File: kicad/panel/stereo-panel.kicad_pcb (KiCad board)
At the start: 2 copper layers, 134.1 x 137.1 mm, 235 parts, among them J1 AC IN 12-15V, J1 DC 12V IN, J1 IN L-G-R, J2 DC IN 12V, J2 IN L-G-R, J2 OUT L-G-R, J3 DC OUT 1, J3 LED IN, J3 SPK L, J4 DC OUT 2, J4 SPK R, J5 LED REMOTE, Q1 BC547, Q1001 BC547, Q1002 BC547, Q1003 BC557, Q1004 BD139, Q1005 BD140, Q1006 BC547, Q2 TIP41C, Q2001 BC547, Q2002 BC547, Q2003 BC557, Q2004 BD139, Q2005 BD140, Q2006 BC547, Q3 BC547

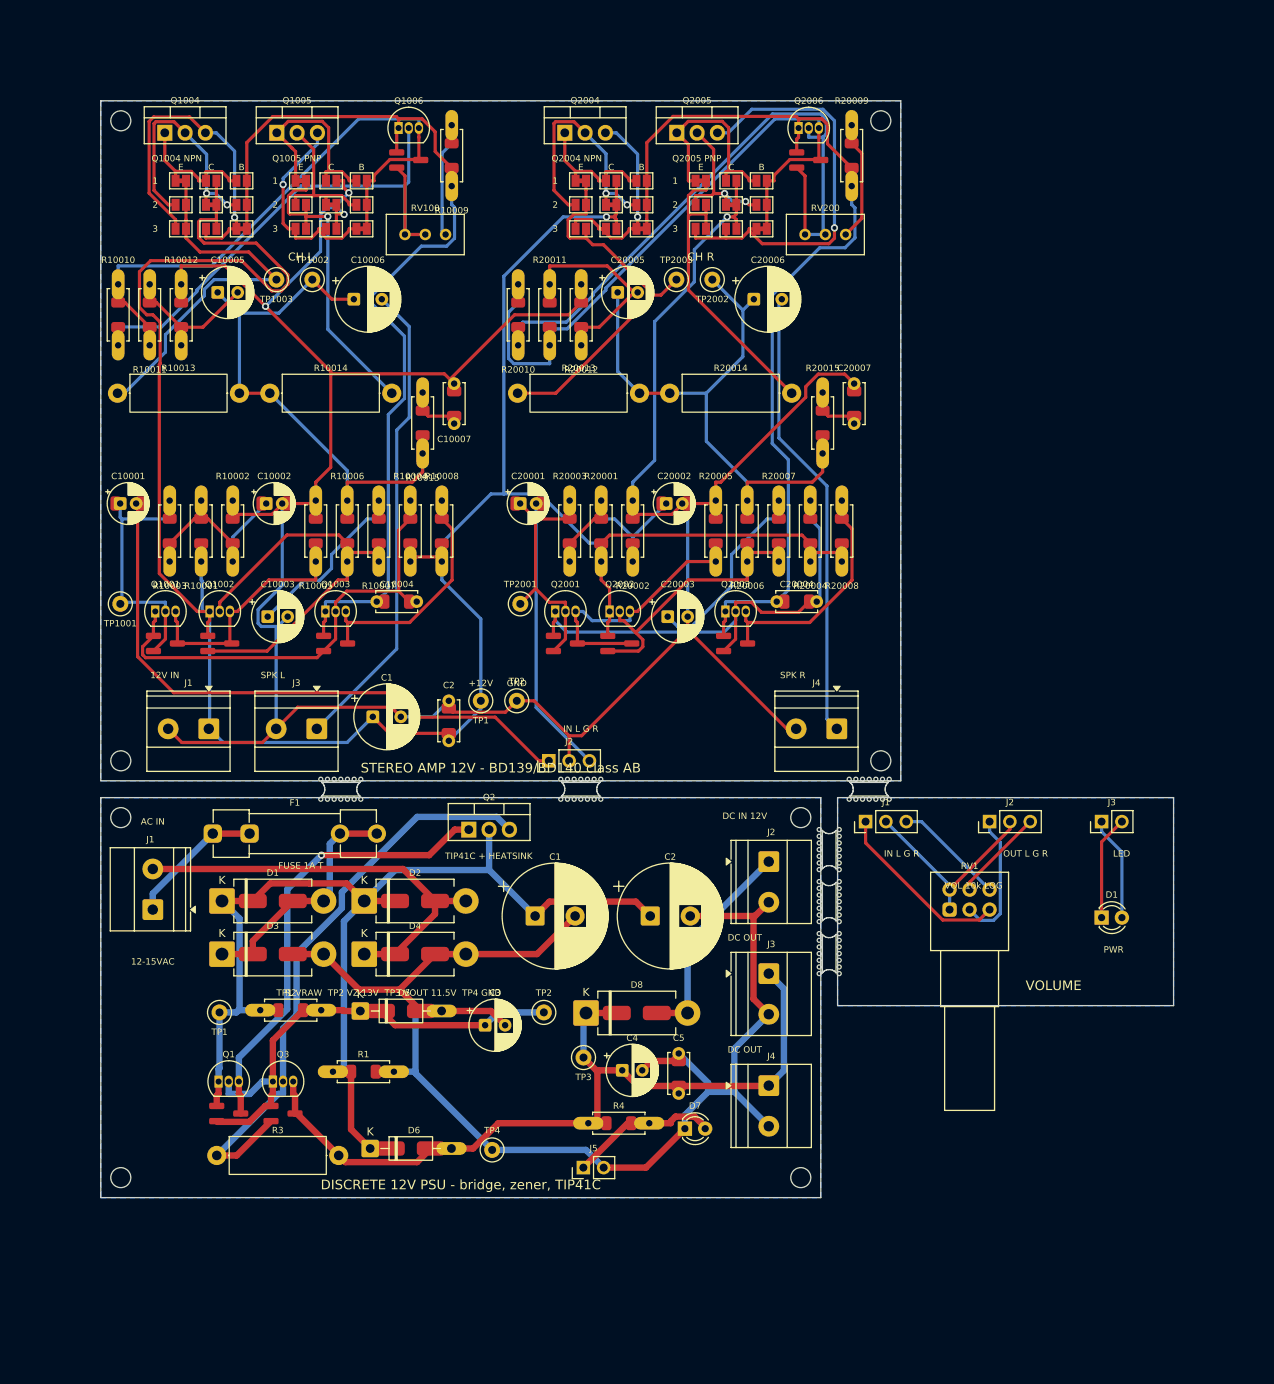
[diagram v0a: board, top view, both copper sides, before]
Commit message: Rotate screw terminals to face the board edge, add 3D views, schematics and layouts to the README, CircuitJS links in the review
Amp board is 100 x 85 mm after the hybrid-footprint courtyards grew; input header moved to open space
on the bottom edge so freerouting completes. Panel 134 x 137 mm, DRC clean.
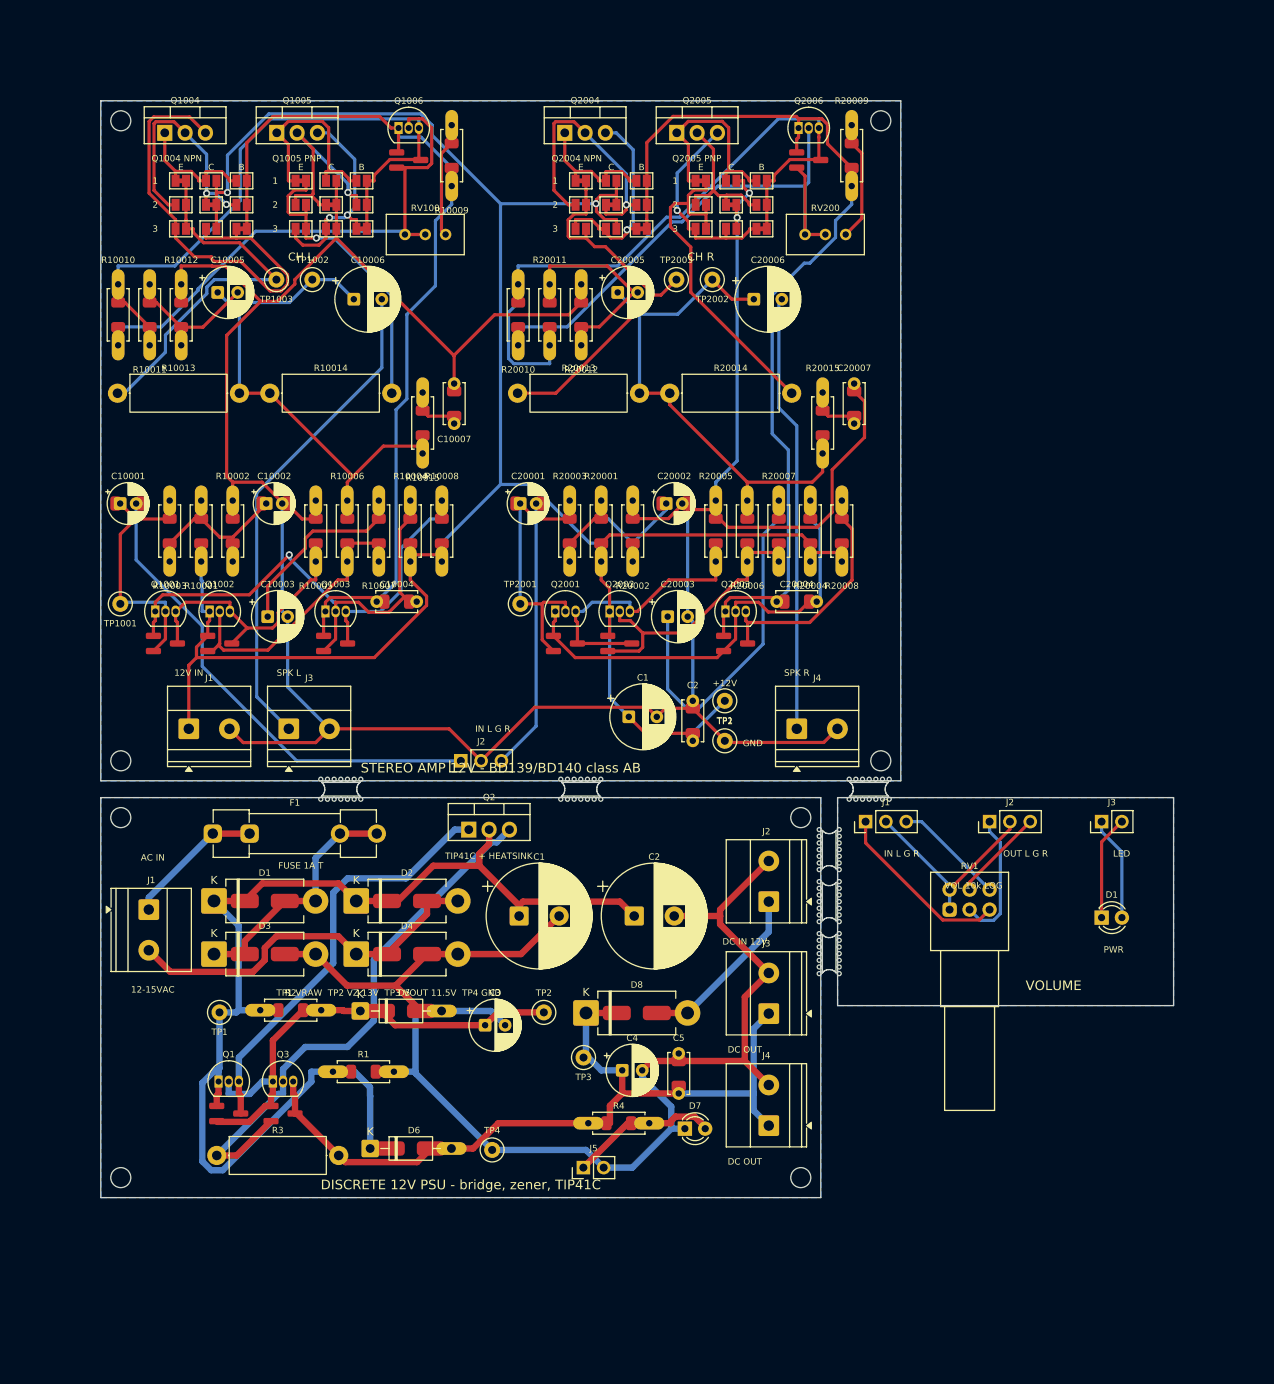
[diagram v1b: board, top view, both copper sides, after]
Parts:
- removed the C1 at (34.0, 77.0)
- removed the C1 at (54.3, 101.9)
- removed the C2 at (43.5, 80.0)
- removed the C2 at (68.7, 101.9)
- removed the J1 at (6.50, 101.1)
- removed the J1 at (13.5, 78.5)
- removed the J2 at (56.0, 82.5)
- removed the J2 at (83.5, 95.1)
- removed the J3 at (83.5, 109.1)
- removed the J3 at (27.0, 78.5)
- removed the J4 at (83.5, 123.1)
- removed the J4 at (92.0, 78.5)
- added C1: 1000u, Capacitor_THT:CP_Radial_D8.0mm_P3.50mm, F.Cu at (66.0, 77.0)
- added C1: 2200u, Capacitor_THT:CP_Radial_D13.0mm_P5.00mm, F.Cu at (52.3, 101.9)
- added C2: 2200u, Capacitor_THT:CP_Radial_D13.0mm_P5.00mm, F.Cu at (66.7, 101.9)
- added C2: 100n, Custom:C_P5_1206, F.Cu at (74.0, 80.0)
- added J1: AC IN 12-15V, TerminalBlock_Phoenix:TerminalBlock_Phoenix_MKDS-1,5-2-5.08_1x02_P5.08mm_Horizontal, F.Cu at (6.00, 101.1)
- added J1: DC 12V IN, TerminalBlock_Phoenix:TerminalBlock_Phoenix_MKDS-1,5-2-5.08_1x02_P5.08mm_Horizontal, F.Cu at (11.0, 78.5)
- added J2: IN L-G-R, Connector_PinHeader_2.54mm:PinHeader_1x03_P2.54mm_Vertical, F.Cu at (45.0, 82.5)
- added J2: DC IN 12V, TerminalBlock_Phoenix:TerminalBlock_Phoenix_MKDS-1,5-2-5.08_1x02_P5.08mm_Horizontal, F.Cu at (83.5, 100.1)
- added J3: DC OUT 1, TerminalBlock_Phoenix:TerminalBlock_Phoenix_MKDS-1,5-2-5.08_1x02_P5.08mm_Horizontal, F.Cu at (83.5, 114.1)
- added J3: SPK L, TerminalBlock_Phoenix:TerminalBlock_Phoenix_MKDS-1,5-2-5.08_1x02_P5.08mm_Horizontal, F.Cu at (23.5, 78.5)
- added J4: SPK R, TerminalBlock_Phoenix:TerminalBlock_Phoenix_MKDS-1,5-2-5.08_1x02_P5.08mm_Horizontal, F.Cu at (87.0, 78.5)
- added J4: DC OUT 2, TerminalBlock_Phoenix:TerminalBlock_Phoenix_MKDS-1,5-2-5.08_1x02_P5.08mm_Horizontal, F.Cu at (83.5, 128.1)
- moved TP1 30.5 mm to (78.0, 75.0)
- moved TP2 26.5 mm to (78.0, 80.0)
- moved D1 1.00 mm to (14.2, 100.0)
- moved D2 1.00 mm to (31.9, 100.0)
- moved D3 1.00 mm to (14.2, 106.7)
- moved D4 1.00 mm to (31.9, 106.7)
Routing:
- net Board_0-Net-(JP20017-A): track 53.3 -> 26.0 mm
- net Board_0-+12V: track 316.3 -> 292.3 mm, vias 1 -> 2
- net Board_0-Net-(C20003-Pad1): track 26.9 -> 46.5 mm
- net Board_0-Net-(Q1002-B): track 52.9 -> 36.7 mm
- net Board_0-/IN_L: track 76.5 -> 61.5 mm
- net Board_0-Net-(JP10007-A): track 42.8 -> 56.9 mm, vias 1 -> 0
- net Board_0-Net-(Q2006-B): track 83.3 -> 72.5 mm
- net Board_1-Net-(D1-K): track 142.8 -> 152.8 mm
- net Board_0-Net-(JP10011-A): track 19.2 -> 26.8 mm, vias 0 -> 1
- net Board_0-/OUT_R: track 76.3 -> 68.8 mm
- net Board_1-/AC2: track 53.3 -> 47.1 mm
- net Board_1-Net-(Q2-E): track 73.8 -> 68.3 mm
- net Board_0-Net-(Q1001-C): track 59.1 -> 64.4 mm, vias 0 -> 1
- net Board_1-Net-(D8-A): track 27.0 -> 22.0 mm
- net Board_0-/VAS_L: track 121.5 -> 116.8 mm
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
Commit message: Square 144 x 144 mm panel with rails; amp widened to 134 x 71 mm so PSU plus volume board match its width; readable silkscreen
References sit inside resistor, diode and ceramic outlines along the body axis, larger text; electrolytic,
transistor and test-point labels stay beside the part. Hybrid footprints built from the library parts keep
polarity marks. All 2-layer boards, the panel and the single-sided PSU and volume boards are DRC clean.
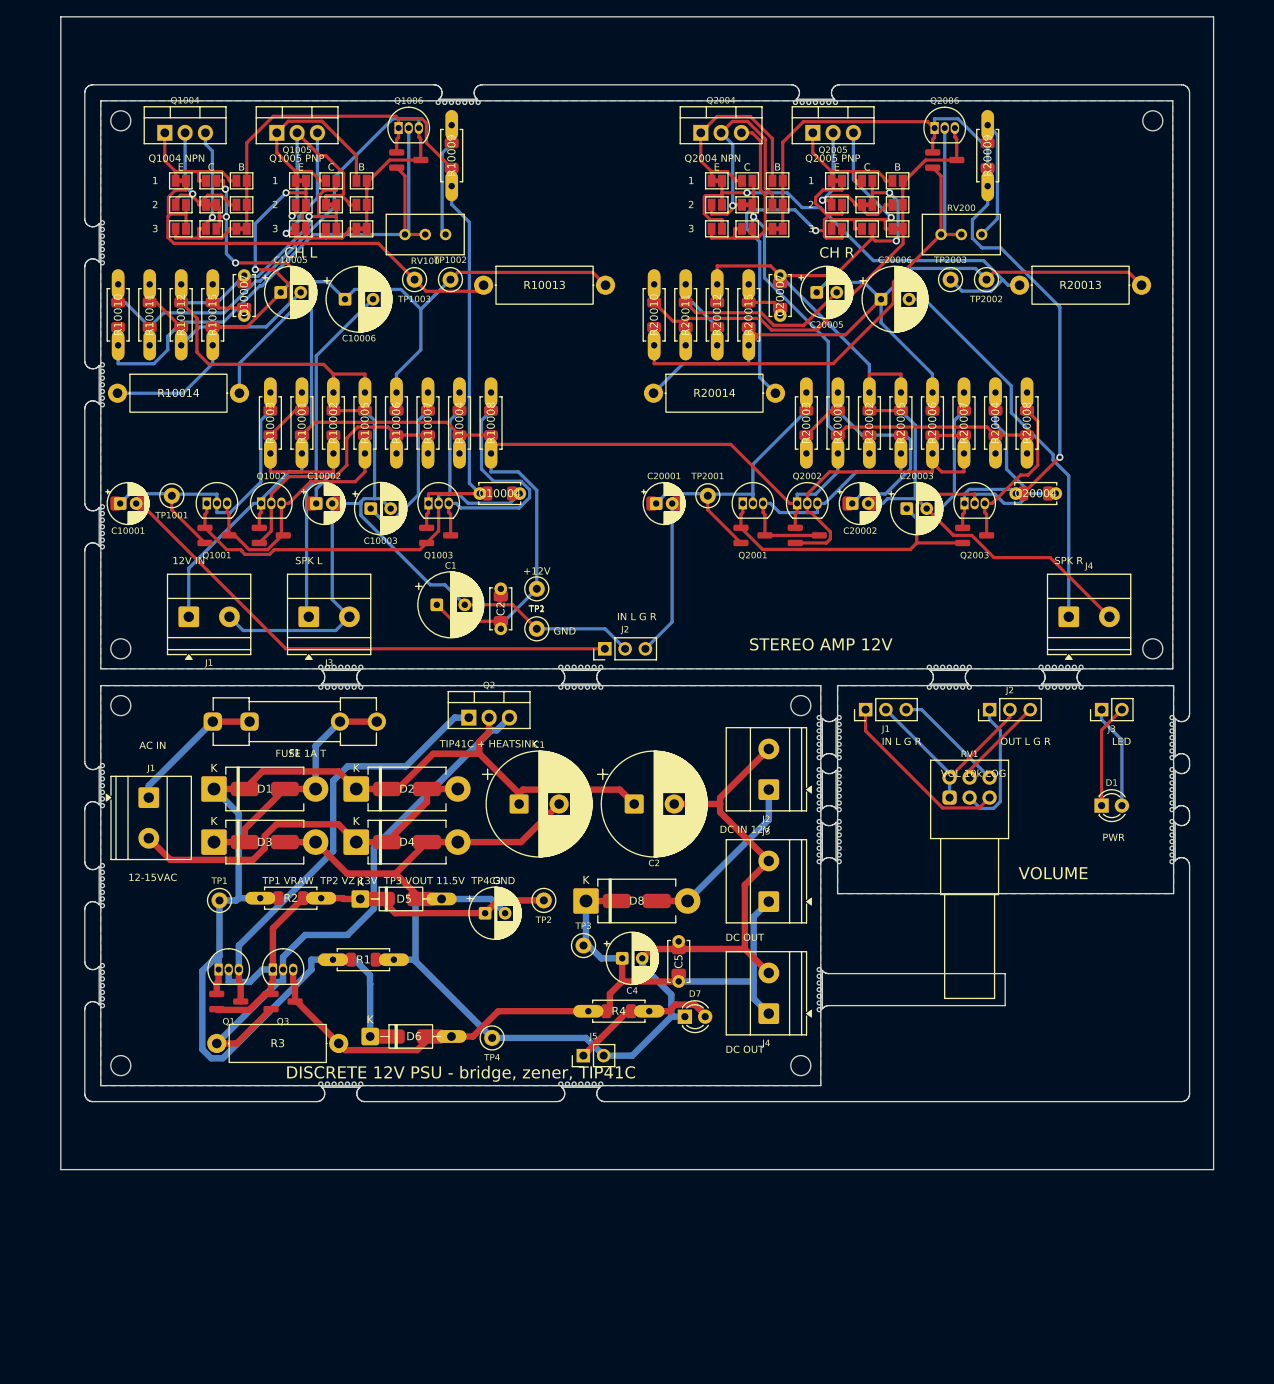
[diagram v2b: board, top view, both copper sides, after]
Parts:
- removed the C1 at (66.0, 77.0)
- removed the C1 at (52.3, 101.9)
- removed the C2 at (66.7, 101.9)
- removed the C2 at (74.0, 80.0)
- removed the D1 at (14.2, 100.0)
- removed the D1 at (125.1, 102.1)
- removed the H2 at (87.5, 89.6)
- removed the H2 at (97.5, 2.50)
- removed the H3 at (2.50, 82.5)
- removed the H3 at (2.50, 134.6)
- removed the H4 at (87.5, 134.6)
- removed the H4 at (97.5, 82.5)
- removed the J1 at (6.00, 101.1)
- removed the J1 at (11.0, 78.5)
- removed the J1 at (95.6, 90.1)
- removed the J2 at (111.1, 90.1)
- removed the J2 at (45.0, 82.5)
- removed the J2 at (83.5, 100.1)
- removed the J3 at (125.1, 90.1)
- removed the J3 at (83.5, 114.1)
- removed the J3 at (23.5, 78.5)
- removed the J4 at (87.0, 78.5)
- removed the J4 at (83.5, 128.1)
- removed the TP1 at (14.8, 114.0)
- removed the TP1 at (78.0, 75.0)
- removed the TP2 at (78.0, 80.0)
- removed the TP2 at (55.4, 114.0)
- added C1: 2200u, Capacitor_THT:CP_Radial_D13.0mm_P5.00mm, F.Cu at (52.3, 87.9)
- added C1: 1000u, Capacitor_THT:CP_Radial_D8.0mm_P3.50mm, F.Cu at (42.0, 63.0)
- added C2: 2200u, Capacitor_THT:CP_Radial_D13.0mm_P5.00mm, F.Cu at (66.7, 87.9)
- added C2: 100n, Custom:C_P5_1206, F.Cu at (50.0, 66.0)
- added D1: POWER LED, LED_THT:LED_D3.0mm, F.Cu at (125.1, 88.1)
- added D1: 1N5401, Custom:D_DO201_SMA, F.Cu at (14.2, 86.0)
- added H2: M2.5, Custom:Hole_2.5mm, F.Cu at (87.5, 75.6)
- added H2: M2.5, Custom:Hole_2.5mm, F.Cu at (131.5, 2.50)
- added H3: M2.5, Custom:Hole_2.5mm, F.Cu at (2.50, 68.5)
- added H3: M2.5, Custom:Hole_2.5mm, F.Cu at (2.50, 120.6)
- added H4: M2.5, Custom:Hole_2.5mm, F.Cu at (87.5, 120.6)
- added H4: M2.5, Custom:Hole_2.5mm, F.Cu at (131.5, 68.5)
- added J1: DC 12V IN, TerminalBlock_Phoenix:TerminalBlock_Phoenix_MKDS-1,5-2-5.08_1x02_P5.08mm_Horizontal, F.Cu at (11.0, 64.5)
- added J1: AC IN 12-15V, TerminalBlock_Phoenix:TerminalBlock_Phoenix_MKDS-1,5-2-5.08_1x02_P5.08mm_Horizontal, F.Cu at (6.00, 87.1)
- added J1: IN L-G-R, Connector_PinHeader_2.54mm:PinHeader_1x03_P2.54mm_Vertical, F.Cu at (95.6, 76.1)
- added J2: OUT L-G-R, Connector_PinHeader_2.54mm:PinHeader_1x03_P2.54mm_Vertical, F.Cu at (111.1, 76.1)
- added J2: IN L-G-R, Connector_PinHeader_2.54mm:PinHeader_1x03_P2.54mm_Vertical, F.Cu at (63.0, 68.5)
- added J2: DC IN 12V, TerminalBlock_Phoenix:TerminalBlock_Phoenix_MKDS-1,5-2-5.08_1x02_P5.08mm_Horizontal, F.Cu at (83.5, 86.1)
- added J3: DC OUT 1, TerminalBlock_Phoenix:TerminalBlock_Phoenix_MKDS-1,5-2-5.08_1x02_P5.08mm_Horizontal, F.Cu at (83.5, 100.1)
- added J3: LED IN, Connector_PinHeader_2.54mm:PinHeader_1x02_P2.54mm_Vertical, F.Cu at (125.1, 76.1)
- added J3: SPK L, TerminalBlock_Phoenix:TerminalBlock_Phoenix_MKDS-1,5-2-5.08_1x02_P5.08mm_Horizontal, F.Cu at (26.0, 64.5)
- added J4: DC OUT 2, TerminalBlock_Phoenix:TerminalBlock_Phoenix_MKDS-1,5-2-5.08_1x02_P5.08mm_Horizontal, F.Cu at (83.5, 114.1)
- added J4: SPK R, TerminalBlock_Phoenix:TerminalBlock_Phoenix_MKDS-1,5-2-5.08_1x02_P5.08mm_Horizontal, F.Cu at (121.0, 64.5)
- added KiKit_MB_13_1: NPTH, NPTH, F.Cu at (89.8, 77.1)
- added KiKit_MB_13_2: NPTH, NPTH, F.Cu at (89.8, 77.9)
- added KiKit_MB_13_3: NPTH, NPTH, F.Cu at (89.8, 78.8)
- added KiKit_MB_13_4: NPTH, NPTH, F.Cu at (89.8, 79.6)
- added KiKit_MB_13_5: NPTH, NPTH, F.Cu at (89.8, 80.4)
- added KiKit_MB_13_6: NPTH, NPTH, F.Cu at (89.8, 81.3)
- added KiKit_MB_13_7: NPTH, NPTH, F.Cu at (89.8, 82.1)
- added KiKit_MB_14_1: NPTH, NPTH, F.Cu at (89.8, 83.6)
- added KiKit_MB_14_2: NPTH, NPTH, F.Cu at (89.8, 84.4)
- added KiKit_MB_14_3: NPTH, NPTH, F.Cu at (89.8, 85.3)
- added KiKit_MB_14_4: NPTH, NPTH, F.Cu at (89.8, 86.1)
- added KiKit_MB_14_5: NPTH, NPTH, F.Cu at (89.8, 86.9)
- added KiKit_MB_14_6: NPTH, NPTH, F.Cu at (89.8, 87.8)
- added KiKit_MB_14_7: NPTH, NPTH, F.Cu at (89.8, 88.6)
- added KiKit_MB_15_1: NPTH, NPTH, F.Cu at (89.8, 90.1)
- added KiKit_MB_15_2: NPTH, NPTH, F.Cu at (89.8, 90.9)
- added KiKit_MB_15_3: NPTH, NPTH, F.Cu at (89.8, 91.8)
- added KiKit_MB_15_4: NPTH, NPTH, F.Cu at (89.8, 92.6)
- added KiKit_MB_15_5: NPTH, NPTH, F.Cu at (89.8, 93.4)
- added KiKit_MB_15_6: NPTH, NPTH, F.Cu at (89.8, 94.3)
- added KiKit_MB_15_7: NPTH, NPTH, F.Cu at (89.8, 95.1)
- added KiKit_MB_16_1: NPTH, NPTH, F.Cu at (89.8, 108.6)
- added KiKit_MB_16_2: NPTH, NPTH, F.Cu at (89.8, 109.4)
- added KiKit_MB_16_3: NPTH, NPTH, F.Cu at (89.8, 110.3)
- added KiKit_MB_16_4: NPTH, NPTH, F.Cu at (89.8, 111.1)
- added KiKit_MB_16_5: NPTH, NPTH, F.Cu at (89.8, 111.9)
- added KiKit_MB_16_6: NPTH, NPTH, F.Cu at (89.8, 112.8)
- added KiKit_MB_16_7: NPTH, NPTH, F.Cu at (89.8, 113.6)
- added KiKit_MB_17_1: NPTH, NPTH, F.Cu at (27.5, 73.3)
- added KiKit_MB_17_2: NPTH, NPTH, F.Cu at (28.3, 73.3)
- added KiKit_MB_17_3: NPTH, NPTH, F.Cu at (29.2, 73.3)
- added KiKit_MB_17_4: NPTH, NPTH, F.Cu at (30.0, 73.3)
- added KiKit_MB_17_5: NPTH, NPTH, F.Cu at (30.8, 73.3)
- added KiKit_MB_17_6: NPTH, NPTH, F.Cu at (31.7, 73.3)
- added KiKit_MB_17_7: NPTH, NPTH, F.Cu at (32.5, 73.3)
- added KiKit_MB_18_1: NPTH, NPTH, F.Cu at (57.5, 73.3)
- added KiKit_MB_18_2: NPTH, NPTH, F.Cu at (58.3, 73.3)
- added KiKit_MB_18_3: NPTH, NPTH, F.Cu at (59.2, 73.3)
- added KiKit_MB_18_4: NPTH, NPTH, F.Cu at (60.0, 73.3)
- added KiKit_MB_18_5: NPTH, NPTH, F.Cu at (60.8, 73.3)
- added KiKit_MB_18_6: NPTH, NPTH, F.Cu at (61.7, 73.3)
- added KiKit_MB_18_7: NPTH, NPTH, F.Cu at (62.5, 73.3)
- added KiKit_MB_19_1: NPTH, NPTH, F.Cu at (32.5, 122.9)
- added KiKit_MB_19_2: NPTH, NPTH, F.Cu at (31.7, 122.9)
- added KiKit_MB_19_3: NPTH, NPTH, F.Cu at (30.8, 122.9)
- added KiKit_MB_19_4: NPTH, NPTH, F.Cu at (30.0, 122.9)
- added KiKit_MB_19_5: NPTH, NPTH, F.Cu at (29.2, 122.9)
- added KiKit_MB_19_6: NPTH, NPTH, F.Cu at (28.3, 122.9)
- added KiKit_MB_19_7: NPTH, NPTH, F.Cu at (27.5, 122.9)
- added KiKit_MB_20_1: NPTH, NPTH, F.Cu at (62.5, 122.9)
- added KiKit_MB_20_2: NPTH, NPTH, F.Cu at (61.7, 122.9)
- added KiKit_MB_20_3: NPTH, NPTH, F.Cu at (60.8, 122.9)
- added KiKit_MB_20_4: NPTH, NPTH, F.Cu at (60.0, 122.9)
- added KiKit_MB_20_5: NPTH, NPTH, F.Cu at (59.2, 122.9)
- added KiKit_MB_20_6: NPTH, NPTH, F.Cu at (58.3, 122.9)
- added KiKit_MB_20_7: NPTH, NPTH, F.Cu at (57.5, 122.9)
- added KiKit_MB_21_1: NPTH, NPTH, F.Cu at (92.3, 82.1)
- added KiKit_MB_21_2: NPTH, NPTH, F.Cu at (92.3, 81.3)
- added KiKit_MB_21_3: NPTH, NPTH, F.Cu at (92.3, 80.4)
- added KiKit_MB_21_4: NPTH, NPTH, F.Cu at (92.3, 79.6)
- added KiKit_MB_21_5: NPTH, NPTH, F.Cu at (92.3, 78.8)
- added KiKit_MB_21_6: NPTH, NPTH, F.Cu at (92.3, 77.9)
- added KiKit_MB_21_7: NPTH, NPTH, F.Cu at (92.3, 77.1)
- added KiKit_MB_22_1: NPTH, NPTH, F.Cu at (92.3, 88.6)
- added KiKit_MB_22_2: NPTH, NPTH, F.Cu at (92.3, 87.8)
- added KiKit_MB_22_3: NPTH, NPTH, F.Cu at (92.3, 86.9)
- added KiKit_MB_22_4: NPTH, NPTH, F.Cu at (92.3, 86.1)
- added KiKit_MB_22_5: NPTH, NPTH, F.Cu at (92.3, 85.3)
- added KiKit_MB_22_6: NPTH, NPTH, F.Cu at (92.3, 84.4)
- added KiKit_MB_22_7: NPTH, NPTH, F.Cu at (92.3, 83.6)
- added KiKit_MB_23_1: NPTH, NPTH, F.Cu at (92.3, 95.1)
- added KiKit_MB_23_2: NPTH, NPTH, F.Cu at (92.3, 94.3)
- added KiKit_MB_23_3: NPTH, NPTH, F.Cu at (92.3, 93.4)
- added KiKit_MB_23_4: NPTH, NPTH, F.Cu at (92.3, 92.6)
- added KiKit_MB_23_5: NPTH, NPTH, F.Cu at (92.3, 91.8)
- added KiKit_MB_23_6: NPTH, NPTH, F.Cu at (92.3, 90.9)
- added KiKit_MB_23_7: NPTH, NPTH, F.Cu at (92.3, 90.1)
- added KiKit_MB_24_1: NPTH, NPTH, F.Cu at (133.9, 77.1)
- added KiKit_MB_24_2: NPTH, NPTH, F.Cu at (133.9, 77.9)
- added KiKit_MB_24_3: NPTH, NPTH, F.Cu at (133.9, 78.8)
- added KiKit_MB_24_4: NPTH, NPTH, F.Cu at (133.9, 79.6)
- added KiKit_MB_24_5: NPTH, NPTH, F.Cu at (133.9, 80.4)
- added KiKit_MB_24_6: NPTH, NPTH, F.Cu at (133.9, 81.3)
- added KiKit_MB_24_7: NPTH, NPTH, F.Cu at (133.9, 82.1)
- added KiKit_MB_25_1: NPTH, NPTH, F.Cu at (133.9, 83.6)
- added KiKit_MB_25_2: NPTH, NPTH, F.Cu at (133.9, 84.4)
- added KiKit_MB_25_3: NPTH, NPTH, F.Cu at (133.9, 85.3)
- added KiKit_MB_25_4: NPTH, NPTH, F.Cu at (133.9, 86.1)
- added KiKit_MB_25_5: NPTH, NPTH, F.Cu at (133.9, 86.9)
- added KiKit_MB_25_6: NPTH, NPTH, F.Cu at (133.9, 87.8)
- added KiKit_MB_25_7: NPTH, NPTH, F.Cu at (133.9, 88.6)
- added KiKit_MB_26_1: NPTH, NPTH, F.Cu at (133.9, 90.1)
- added KiKit_MB_26_2: NPTH, NPTH, F.Cu at (133.9, 90.9)
- added KiKit_MB_26_3: NPTH, NPTH, F.Cu at (133.9, 91.8)
- added KiKit_MB_26_4: NPTH, NPTH, F.Cu at (133.9, 92.6)
- added KiKit_MB_26_5: NPTH, NPTH, F.Cu at (133.9, 93.4)
- added KiKit_MB_26_6: NPTH, NPTH, F.Cu at (133.9, 94.3)
- added KiKit_MB_26_7: NPTH, NPTH, F.Cu at (133.9, 95.1)
- added KiKit_MB_27_1: NPTH, NPTH, F.Cu at (103.6, 73.3)
- added KiKit_MB_27_2: NPTH, NPTH, F.Cu at (104.4, 73.3)
- added KiKit_MB_27_3: NPTH, NPTH, F.Cu at (105.2, 73.3)
- added KiKit_MB_27_4: NPTH, NPTH, F.Cu at (106.1, 73.3)
- added KiKit_MB_27_5: NPTH, NPTH, F.Cu at (106.9, 73.3)
- added KiKit_MB_27_6: NPTH, NPTH, F.Cu at (107.7, 73.3)
- added KiKit_MB_27_7: NPTH, NPTH, F.Cu at (108.6, 73.3)
- added KiKit_MB_28_1: NPTH, NPTH, F.Cu at (117.5, 73.3)
- added KiKit_MB_28_2: NPTH, NPTH, F.Cu at (118.4, 73.3)
- added KiKit_MB_28_3: NPTH, NPTH, F.Cu at (119.2, 73.3)
- added KiKit_MB_28_4: NPTH, NPTH, F.Cu at (120.0, 73.3)
- added KiKit_MB_28_5: NPTH, NPTH, F.Cu at (120.9, 73.3)
- added KiKit_MB_28_6: NPTH, NPTH, F.Cu at (121.7, 73.3)
- added KiKit_MB_28_7: NPTH, NPTH, F.Cu at (122.5, 73.3)
- added TP1: +12V, TestPoint:TestPoint_Loop_D2.50mm_Drill1.0mm, F.Cu at (54.5, 61.0)
- added TP1: VRAW 14-19V, TestPoint:TestPoint_Loop_D2.50mm_Drill1.0mm, F.Cu at (14.8, 100.0)
- added TP2: VZ 13V, TestPoint:TestPoint_Loop_D2.50mm_Drill1.0mm, F.Cu at (55.4, 100.0)
- added TP2: GND, TestPoint:TestPoint_Loop_D2.50mm_Drill1.0mm, F.Cu at (54.5, 66.0)
- moved KiKit_MB_4_7 104.9 mm to (47.2, 0.20)
- moved KiKit_MB_4_6 104.5 mm to (46.3, 0.20)
- moved KiKit_MB_4_5 104.1 mm to (45.5, 0.20)
- moved KiKit_MB_4_4 103.7 mm to (44.7, 0.20)
- moved KiKit_MB_4_3 103.4 mm to (43.8, 0.20)
- moved KiKit_MB_4_2 103.0 mm to (43.0, 0.20)
- moved KiKit_MB_4_1 102.6 mm to (42.2, 0.20)
- moved KiKit_MB_3_1 102.6 mm to (0.20, 55.8)
- moved KiKit_MB_5_7 102.4 mm to (91.8, 0.20)
- moved KiKit_MB_3_2 102.0 mm to (0.20, 54.9)
- moved KiKit_MB_5_6 101.6 mm to (91.0, 0.20)
- moved KiKit_MB_3_3 101.4 mm to (0.20, 54.1)
- moved KiKit_MB_3_4 100.9 mm to (0.20, 53.2)
- moved KiKit_MB_5_5 100.7 mm to (90.2, 0.20)
- moved KiKit_MB_12_7 100.5 mm to (0.20, 108.1)
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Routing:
- net Board_0-GND: track 365.0 -> 305.2 mm, vias 2 -> 3
- net Board_0-Net-(JP10007-A): track 56.9 -> 24.2 mm, vias 0 -> 1
- net Board_0-/OUT_R: track 68.8 -> 98.0 mm
- net Board_0-/B5_R: track 88.9 -> 63.3 mm
- net Board_0-Net-(C20003-Pad1): track 46.5 -> 23.2 mm
- net Board_0-/OUT_L: track 67.7 -> 88.4 mm
- net Board_0-/SPK_L: track 61.8 -> 43.3 mm
- net Board_0-+12V: track 292.3 -> 274.7 mm, vias 2 -> 5
- net Board_0-/VAS_L: track 116.8 -> 100.0 mm
- net Board_0-Net-(Q2001-C): track 59.4 -> 76.0 mm
- net Board_0-/IN_R: track 34.5 -> 20.1 mm
- net Board_0-Net-(JP10004-A): track 30.8 -> 19.3 mm, vias 2 -> 1
- net Board_0-Net-(C20002-Pad1): track 29.0 -> 40.4 mm
- net Board_0-/E4_R: track 49.3 -> 60.7 mm, vias 0 -> 1
- net Board_0-Net-(JP20001-A): track 16.5 -> 27.2 mm
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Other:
- board size 134.1 x 137.1 mm -> 144.1 x 144.1 mm
- board text added: "STEREO AMP 12V"
- board text removed: "STEREO AMP 12V - BD139/BD140 class AB"

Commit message: Repository URL and revision on every silkscreen and on the panel rails
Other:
- board text added: "STEREO AMP + PSU + VOLUME v1.0 2026-10 CC BY-NC-SA 4.0"
- board text added: "STEREO AMP 12V v1.0 2026-10"
- board text added: "discrete-stereo-amp v1.0 2026-10"
- board text added: "github.com/lahirunirmalx/discrete-stereo-amp"
- board text added: "github.com/lahirunirmalx/discrete-stereo-amp v1.0 2026-10"
- board text added: "v1.0 2026-10"
- board text removed: "STEREO AMP 12V"
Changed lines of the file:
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@@
 		(layer "Edge.Cuts")
+	)
+	(gr_text "discrete-stereo-amp v1.0 2026-10"
+		(at 62.950546 69.550271 0)
+		(layer "F.SilkS")
+		(effects
+			(font
+				(size 0.8 0.8)
+				(thickness 0.12)
+			)
+		)
+	)
+	(gr_text "v1.0 2026-10"
+		(at 118.950546 89.050271 0)
+		(layer "F.SilkS")
+		(effects
+			(font
+				(size 0.8 0.8)
+				(thickness 0.12)
+			)
+		)
+	)
+	(gr_text "github.com/lahirunirmalx/discrete-stereo-amp"
+		(at 95.950546 59.050271 0)
+		(layer "F.SilkS")
+		(effects
+			(font
+				(size 0.9 0.9)
+				(thickness 0.12)
+			)
+		)
 	)
 	(gr_text "AC IN"
@@
 		)
 	)
+	(gr_text "STEREO AMP + PSU + VOLUME  v1.0 2026-10  CC BY-NC-SA 4.0"
+		(at 67.050546 -9.049729 0)
+		(layer "F.SilkS")
+		(effects
+			(font
+				(size 1.5 1.5)
+				(thickness 0.15)
+			)
+		)
+	)
+	(gr_text "github.com/lahirunirmalx/discrete-stereo-amp  v1.0 2026-10"
+		(at 67.050546 132.150271 0)
+		(layer "F.SilkS")
+		(effects
+			(font
+				(size 1.5 1.5)
+				(thickness 0.15)
+			)
+		)
+	)
 	(gr_text "DISCRETE 12V PSU - bridge, zener, TIP41C"
 		(at 45 121.5 0)
@@
 		)
 	)
-	(gr_text "STEREO AMP 12V"
+	(gr_text "STEREO AMP 12V  v1.0 2026-10"
 		(at 90 68 0)
 		(layer "F.SilkS")

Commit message: Release 1.1: square panel, rotated terminals, readable silkscreen, URL and revision stamps
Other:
- board text added: "STEREO AMP + PSU + VOLUME v1.1 2026-10 CC BY-NC-SA 4.0"
- board text added: "STEREO AMP 12V v1.1 2026-10"
- board text added: "discrete-stereo-amp v1.1 2026-10"
- board text added: "github.com/lahirunirmalx/discrete-stereo-amp v1.1 2026-10"
- board text added: "v1.1 2026-10"
- board text removed: "STEREO AMP + PSU + VOLUME v1.0 2026-10 CC BY-NC-SA 4.0"
- board text removed: "STEREO AMP 12V v1.0 2026-10"
- board text removed: "discrete-stereo-amp v1.0 2026-10"
- board text removed: "github.com/lahirunirmalx/discrete-stereo-amp v1.0 2026-10"
- board text removed: "v1.0 2026-10"
